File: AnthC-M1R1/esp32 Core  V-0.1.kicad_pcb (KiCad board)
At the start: 4 copper layers, 85 x 56 mm, 151 parts, among them J1 USB_B_Micro, J13 NEXTION, J2 RS485, J3 CONN, J4 12V, J5 VIN, Q1 2N7002, Q2 2N7002, Q3 S8050, Q4 S8050, Q5 2N7002, Q6 MMBT3904, U1 TPS54331DR, U10 ADS1115IDGS, U11 MCP73812T-420I-OT, U12 MT3540, U13 TPS54331DR, U2 DS1307Z+, U3 AMS1117-3.3, U4 SP3485EN-L/TR, U5 CP2102-GMR_NRND, U6 ESP32-WROOM, U7 HDC2080, U8 ULN2003, U9 LM324DT, Y2 32.768KHz

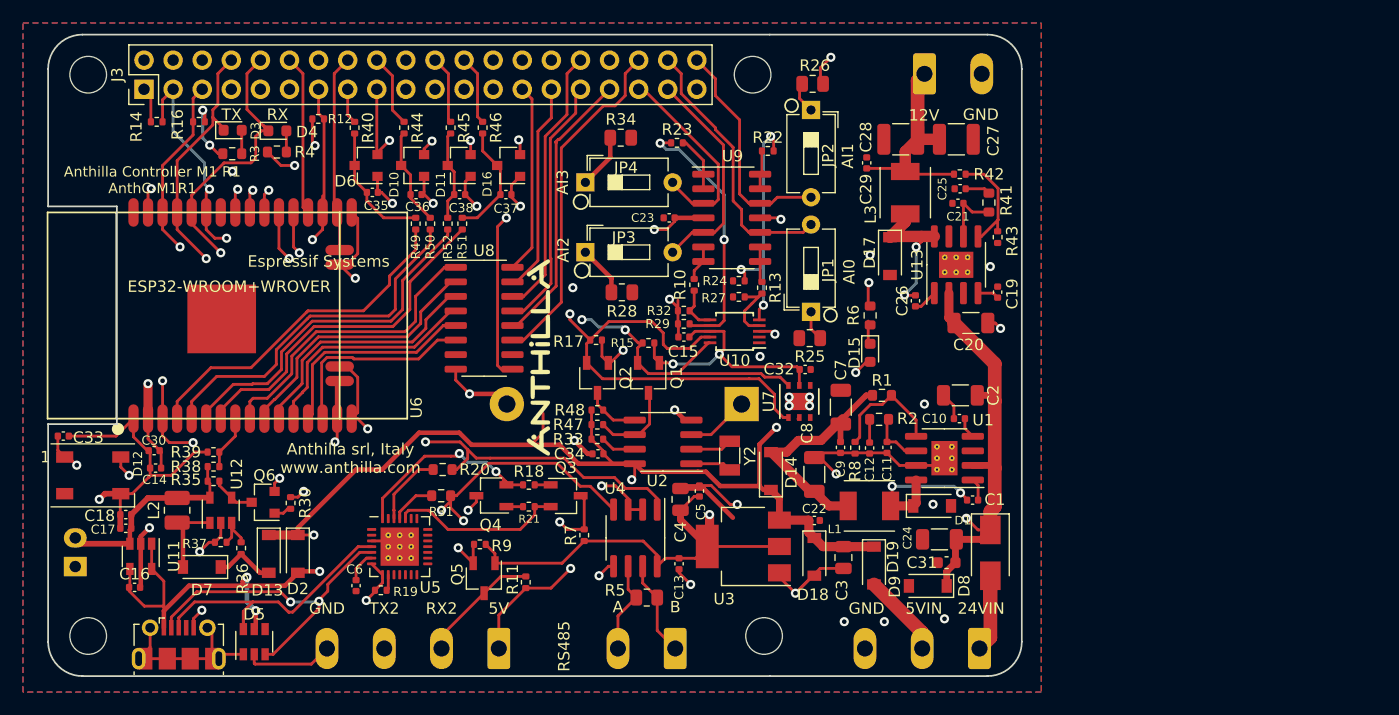
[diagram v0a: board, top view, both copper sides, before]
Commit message: New manufacturing files after emc  modifications
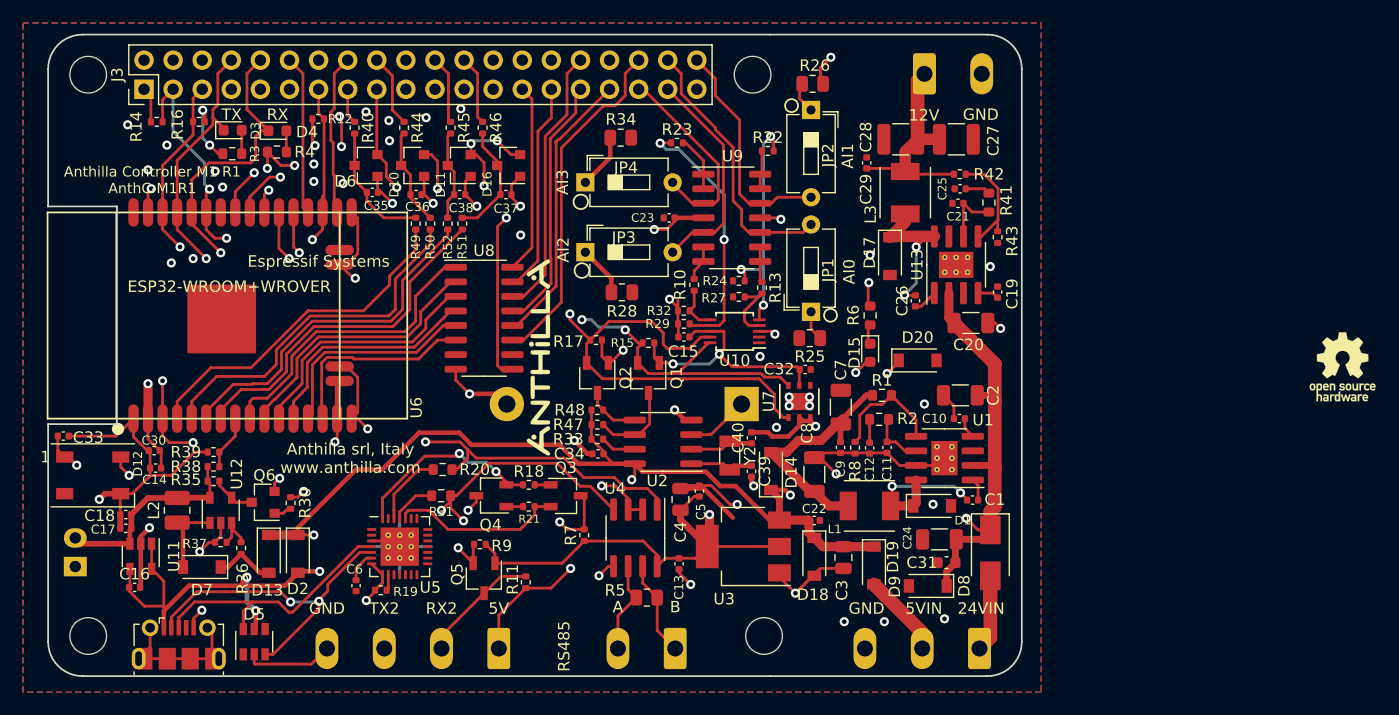
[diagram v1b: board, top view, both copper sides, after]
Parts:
- added C39: 12pF, Capacitor_SMD:C_0402_1005Metric, F.Cu at (241.4, 133.1)
- added C40: 12pF, Capacitor_SMD:C_0402_1005Metric, F.Cu at (241.4, 130.2)
- added D20: B5819W, Diode_SMD:D_SOD-123, F.Cu at (255.9, 123.4)
- added REF**: OSHW-Logo2_14.6x12mm_SilkScreen, Symbol:OSHW-Logo2_14.6x12mm_SilkScreen, B.Cu at (256.0, 110.0)
- added REF**: OSHW-Logo_5.7x6mm_SilkScreen, Symbol:OSHW-Logo_5.7x6mm_SilkScreen, F.Cu at (293.0, 124.0)
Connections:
- D5 pad 1: /SHIELD -> Net-(D5-Pad1)
- J1 pad 6: /SHIELD -> GND
- U7 pad 3: Net-(U7-Pad3) -> GND
- U8 pad 7: Net-(U8-Pad7) -> GND
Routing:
- net GND: track 133.0 -> 220.0 mm, vias 32 -> 51
- net +3V3: track 204.8 -> 240.8 mm, vias 14 -> 15
- net Net-(BT1-Pad1): track 5.49 -> 24.2 mm, vias 0 -> 1
- net /SHIELD: track 14.1 -> 0.00 mm
- net Net-(C39-Pad1): track 3.57 -> 5.62 mm
- net Net-(C40-Pad1): track 3.63 -> 5.61 mm
- net /SCK: track 24.6 -> 25.6 mm
- net /RXD: track 76.3 -> 77.1 mm
- net /CS: track 28.3 -> 29.0 mm
- net +5V: track 226.1 -> 226.6 mm, vias 7 -> 8

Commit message: temperature on board tested
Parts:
- removed the REF** at (293.0, 124.0)
- added C41: 10uF, Capacitor_SMD:C_0402_1005Metric, F.Cu at (197.6, 140.8)
- moved R36 1.00 mm to (197.5, 139.1)
- moved D13 0.61 mm to (199.9, 140.2)
- moved D2 0.61 mm to (202.4, 140.2)
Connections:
- U4 pad 2: /IO13 -> /GPIO0
- U4 pad 3: /IO13 -> /GPIO0
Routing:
- net GND: track 220.0 -> 263.1 mm, vias 51 -> 56
- net /IO13: track 35.1 -> 7.56 mm, vias 2 -> 1
- net /GPIO0: track 46.0 -> 69.0 mm, vias 2 -> 4
- net +5V: track 226.6 -> 228.1 mm
- net Net-(C41-Pad1): track 5.34 -> 6.41 mm
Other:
- board text added: "012"
- board text added: "O14"
- board text added: "O25"
- board text added: "O26"
- board text added: "O27"
